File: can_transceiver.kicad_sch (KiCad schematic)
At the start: 15 parts, among them J5 3.5 mm "CAN" Connector, U7 HMT232T

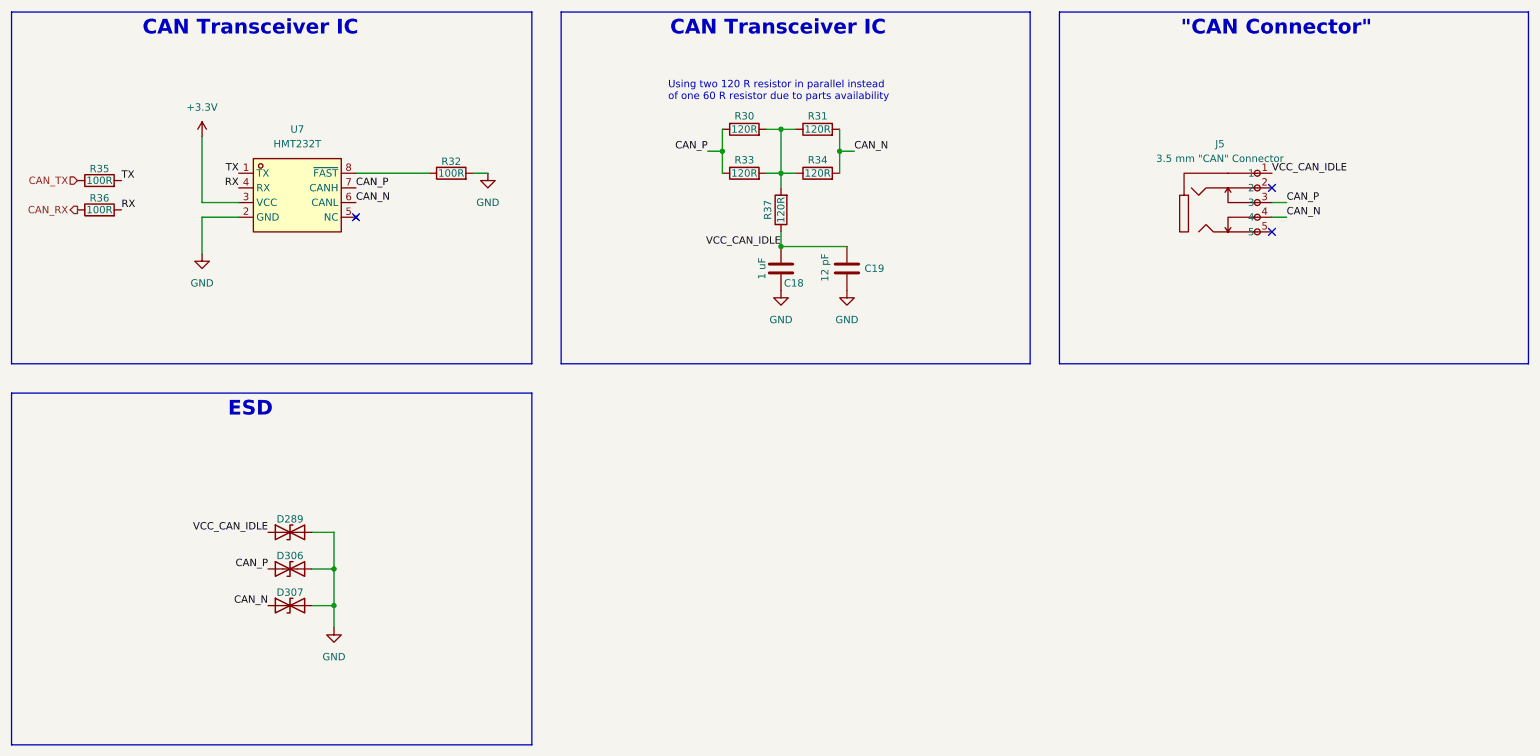
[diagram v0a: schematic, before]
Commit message: Updated badge based on feedback from badge.team
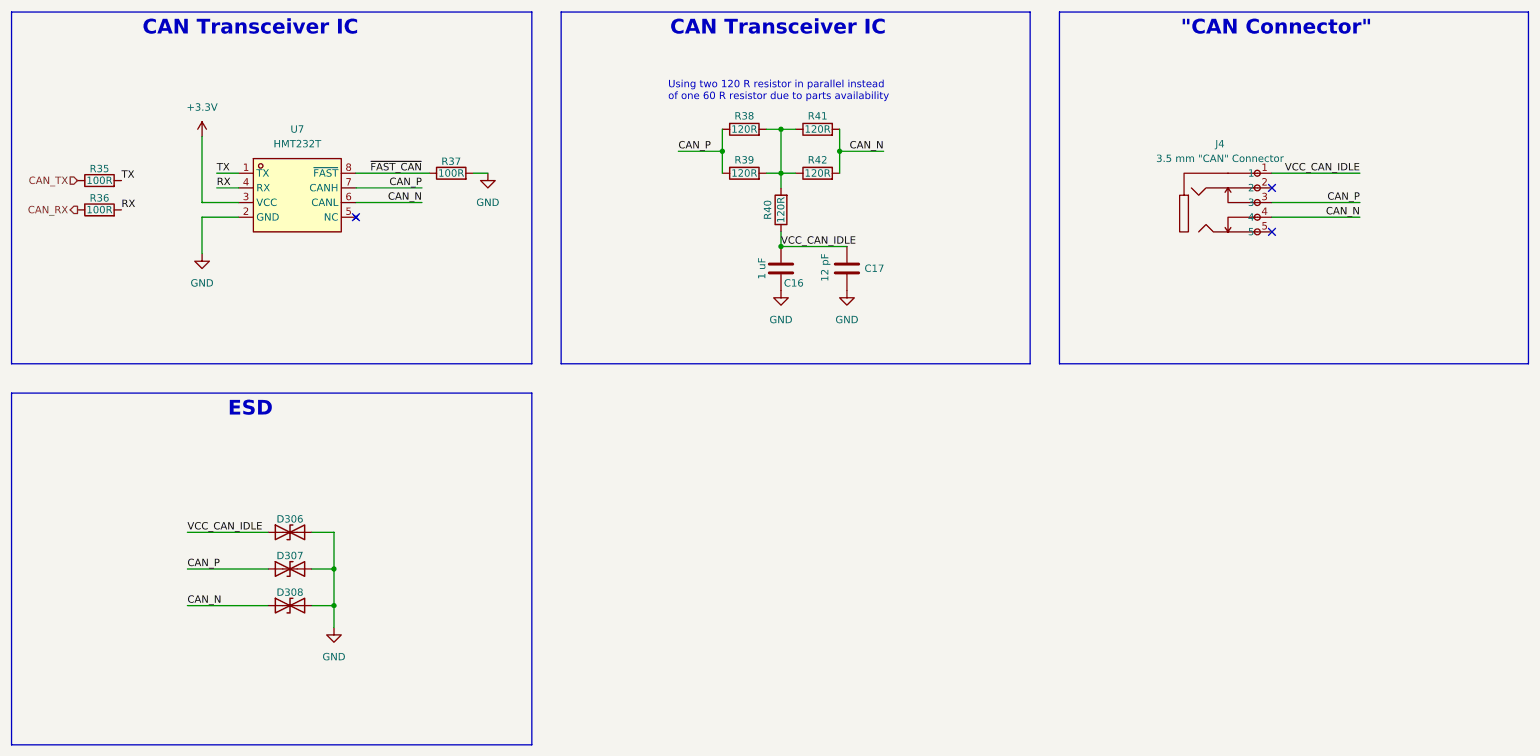
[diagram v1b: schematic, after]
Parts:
- removed D289: D_TVS, custom:DFN0603-2L-BI, symbol Device:D_TVS
- added D308: D_TVS, custom:SOD-882_L1.0-W0.6-BI, symbol Device:D_TVS
- D306, D307: footprint custom:DFN0603-2L-BI -> custom:SOD-882_L1.0-W0.6-BI; LCSC (none) -> C7420372
- renumbered C18 to C16, C19 to C17, J5 to J4, R32 to R37, R30 to R38, R33 to R39, R37 to R40, R31 to R41, R34 to R42
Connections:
- net CAN_N: now also D308.1 (A1); no longer D307.1 (A1)
- net CAN_P: now also D307.1 (A1); no longer D306.1 (A1)
- net GND: now also D308.2 (A2)
- net VCC_CAN_IDLE: now also D306.1 (A1)
- net ~{FAST_CAN}: now reaches R37.1, U7.8 (~{FAST})
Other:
- company: (none) -> Marian Buschsieweke
- title: (none) -> Badge for RIOT Summit '25

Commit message: Schematics: Add accelerometer, drop VBAT sensing
Adding a cheap accelerometer to the boards, sacraficing the VBAT input
to make room for the /CS pin.
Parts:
- removed J4: 3.5 mm "CAN" Connector, custom:AUDIO-TH_PJ324, symbol custom:PJ-3243.5mmAudiosockets
- added J4: 3.5 mm "CAN" Connector, custom:Jack_3.5mm_PJ-320D, symbol Connector_Audio:AudioJack4
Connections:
- net CAN_N: now also J4.T
- net CAN_P: now also J4.R1
- net VCC_CAN_IDLE: now also J4.S
- no-connect marks 3 -> 2
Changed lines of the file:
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@@
-	)
-	(no_connect
-		(at 234.95 54.61)
 	)
 	(no_connect
@@
 	)
 	(symbol
-		(lib_id "custom:PJ-3243.5mmAudiosockets")
-		(at 227.33 48.26 0)
-		(unit 1)
-		(exclude_from_sim no)
-		(in_bom yes)
-		(on_board yes)
-		(dnp no)
-		(fields_autoplaced yes)
-		(property "Reference" "J4"
-			(at 225.935 39.37 0)
-			(effects
-				(font
-					(size 1.27 1.27)
-				)
-			)
-		)
-		(property "Value" "3.5 mm \"CAN\" Connector"
-			(at 225.935 41.91 0)
-			(effects
-				(font
-					(size 1.27 1.27)
-				)
-			)
-		)
-		(property "Footprint" "custom:AUDIO-TH_PJ324"
-			(at 227.33 62.23 0)
-			(effects
-				(font
-					(size 1.27 1.27)
-				)
-				(hide yes)
-			)
-		)
-		(property "Datasheet" "https://lcsc.com/product-detail/Audio-Connectors_PJ-324_C34345.html"
-			(at 227.33 64.77 0)
-			(effects
-				(font
-					(size 1.27 1.27)
-				)
-				(hide yes)
-			)
-		)
-		(property "Description" "3.5 mm Audio Connector"
-			(at 227.33 48.26 0)
-			(effects
-				(font
-					(size 1.27 1.27)
-				)
-				(hide yes)
-			)
-		)
-		(property "LCSC" "C34345"
-			(at 227.33 67.31 0)
-			(effects
-				(font
-					(size 1.27 1.27)
-				)
-				(hide yes)
-			)
-		)
-		(pin "5"
-		)
-		(pin "4"
-		)
-		(pin "3"
-		)
-		(pin "2"
-		)
-		(pin "1"
-		)
-		(instances
-			(project ""
-				(path "/55a8f9ac-2064-4bfa-acf1-805ed6f7ac1b/33b66988-6c10-43b3-b7b0-6637e526ee3e"
-					(reference "J4")
-					(unit 1)
-				)
-			)
-		)
-	)
-	(symbol
 		(lib_id "Device:D_TVS")
 		(at 64.77 119.38 0)
@@
 					(unit 1)
 				)
+			)
+		)
+	)
+	(symbol
+		(lib_id "Connector_Audio:AudioJack4")
+		(at 229.87 46.99 0)
+		(unit 1)
+		(exclude_from_sim no)
+		(in_bom yes)
+		(on_board yes)
+		(dnp no)
+		(fields_autoplaced yes)
+		(property "Reference" "J4"
+			(at 227.33 38.1 0)
+			(effects
+				(font
+					(size 1.27 1.27)
+				)
+			)
+		)
+		(property "Value" "3.5 mm \"CAN\" Connector"
+			(at 227.33 40.64 0)
+			(effects
+				(font
+					(size 1.27 1.27)
+				)
+			)
+		)
+		(property "Footprint" "custom:Jack_3.5mm_PJ-320D"
+			(at 229.87 46.99 0)
+			(effects
+				(font
+					(size 1.27 1.27)
+				)
+				(hide yes)
+			)
+		)
+		(property "Datasheet" "https://jlcpcb.com/api/file/downloadByFileSystemAccessId/8603385968087494656"
+			(at 229.87 46.99 0)
+			(effects
+				(font
+					(size 1.27 1.27)
+				)
+				(hide yes)
+			)
+		)
+		(property "Description" "Audio Jack, 4 Poles (TRRS), abused for CAN"
+			(at 229.87 46.99 0)
+			(effects
+				(font
+					(size 1.27 1.27)
+				)
+				(hide yes)
+			)
+		)
+		(property "LCSC" "C22459515"
+			(at 229.87 46.99 0)
+			(effects
+				(font
+					(size 1.27 1.27)
+				)
+				(hide yes)
+			)
+		)
+		(pin "R1"
+		)
+		(pin "T"
+		)
+		(pin "S"
+		)
+		(pin "R2"
+		)
+		(instances
+			(project ""
+				(path "/55a8f9ac-2064-4bfa-acf1-805ed6f7ac1b/33b66988-6c10-43b3-b7b0-6637e526ee3e"
+					(reference "J4")
+					(unit 1)
+				)
